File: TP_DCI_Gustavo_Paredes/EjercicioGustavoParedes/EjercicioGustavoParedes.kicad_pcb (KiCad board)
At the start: 2 copper layers, 5 parts, among them J1 Conn_01x03

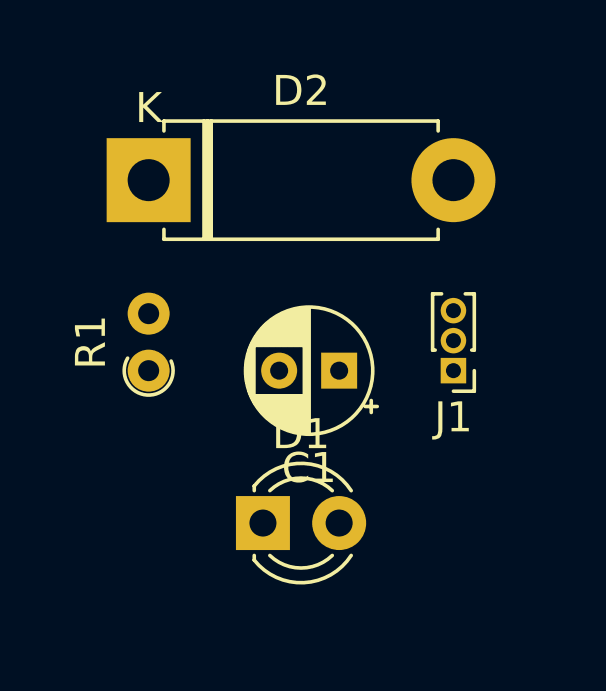
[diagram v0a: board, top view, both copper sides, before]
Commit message: Clase 5 completa
Ruteo, Puente, Recuadro.
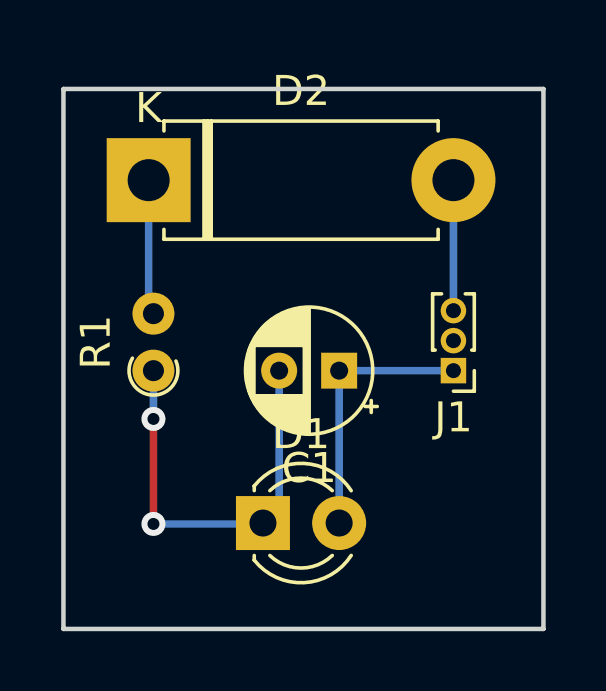
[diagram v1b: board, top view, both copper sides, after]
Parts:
- moved R1 0.16 mm to (117.0, 72.4)
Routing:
- net Net-(C1-Pad2): track 0.00 -> 14.1 mm, vias 0 -> 2
- net Net-(C1-Pad1): track 0.00 -> 8.89 mm
- net Net-(D2-Pad1): track 0.00 -> 4.52 mm
- net Net-(D2-Pad2): track 0.00 -> 4.35 mm
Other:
- board outline added: 16 x 18 mm
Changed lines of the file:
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@@
   (general
     (thickness 1.6)
-    (drawings 0)
-    (tracks 0)
+    (drawings 6)
+    (tracks 13)
     (zones 0)
     (modules 5)
@@
   (setup
     (last_trace_width 0.25)
+    (user_trace_width 0.8)
+    (user_trace_width 1)
+    (user_trace_width 1.2)
     (trace_clearance 0.2)
     (zone_clearance 0.508)
@@
     (via_min_size 0.4)
     (via_min_drill 0.3)
+    (user_via 1.6 0.8)
+    (user_via 2 0.9)
     (uvia_size 0.3)
     (uvia_drill 0.1)
@@
   )
   (module Resistor_THT:R_Axial_DIN0204_L3.6mm_D1.6mm_P1.90mm_Vertical (layer F.Cu)
-    (at 116.84 72.39 90)
+    (at 117 72.39 90)
     (descr "Resistor, Axial_DIN0204 series, Axial, Vertical, pin pitch=1.9mm, 0.167W, length*diameter=3.6*1.6mm^2, http://cdn-reichelt.de/documents/datenblatt/B400/1_4W%23YAG.pdf")
     (tags "Resistor Axial_DIN0204 series Axial Vertical pin pitch 1.9mm 0.167W length 3.6mm diameter 1.6mm")
@@
     )
   )
+  (dimension 16 (width 0.3) (layer Dwgs.User)
+    (gr_text "16,000 mm" (at 122 57.4) (layer Dwgs.User)
+      (effects (font (size 1.5 1.5) (thickness 0.3)))
+    )
+    (feature1 (pts (xy 114 63) (xy 114 58.913579)))
+    (feature2 (pts (xy 130 63) (xy 130 58.913579)))
+    (crossbar (pts (xy 130 59.5) (xy 114 59.5)))
+    (arrow1a (pts (xy 114 59.5) (xy 115.126504 58.913579)))
+    (arrow1b (pts (xy 114 59.5) (xy 115.126504 60.086421)))
+    (arrow2a (pts (xy 130 59.5) (xy 128.873496 58.913579)))
+    (arrow2b (pts (xy 130 59.5) (xy 128.873496 60.086421)))
+  )
+  (dimension 18 (width 0.3) (layer Dwgs.User)
+    (gr_text "18,000 mm" (at 135.6 72 90) (layer Dwgs.User)
+      (effects (font (size 1.5 1.5) (thickness 0.3)))
+    )
+    (feature1 (pts (xy 130 63) (xy 134.086421 63)))
+    (feature2 (pts (xy 130 81) (xy 134.086421 81)))
+    (crossbar (pts (xy 133.5 81) (xy 133.5 63)))
+    (arrow1a (pts (xy 133.5 63) (xy 134.086421 64.126504)))
+    (arrow1b (pts (xy 133.5 63) (xy 132.913579 64.126504)))
+    (arrow2a (pts (xy 133.5 81) (xy 134.086421 79.873496)))
+    (arrow2b (pts (xy 133.5 81) (xy 132.913579 79.873496)))
+  )
+  (gr_line (start 130 81) (end 114 81) (layer Edge.Cuts) (width 0.15))
+  (gr_line (start 130 63) (end 130 81) (layer Edge.Cuts) (width 0.15))
+  (gr_line (start 114 63) (end 130 63) (layer Edge.Cuts) (width 0.15))
+  (gr_line (start 114 81) (end 114 63) (layer Edge.Cuts) (width 0.15))
+  (segment (start 127 72.39) (end 123.19 72.39) (width 0.25) (layer B.Cu) (net 1))
+  (segment (start 123.19 72.39) (end 123.19 77.47) (width 0.25) (layer B.Cu) (net 1))
+  (segment (start 121.19 76.93) (end 120.65 77.47) (width 0.25) (layer B.Cu) (net 2))
+  (segment (start 121.19 72.39) (end 121.19 76.93) (width 0.25) (layer B.Cu) (net 2))
+  (via (at 117 74) (size 0.8) (drill 0.4) (layers F.Cu B.Cu) (net 2))
+  (segment (start 117 72.39) (end 117 74) (width 0.25) (layer B.Cu) (net 2))
+  (via (at 117 77.5) (size 0.8) (drill 0.4) (layers F.Cu B.Cu) (net 2))
+  (segment (start 117 74) (end 117 77.5) (width 0.25) (layer F.Cu) (net 2))
+  (segment (start 120.62 77.5) (end 120.65 77.47) (width 0.25) (layer B.Cu) (net 2))
+  (segment (start 117 77.5) (end 120.62 77.5) (width 0.25) (layer B.Cu) (net 2))
+  (segment (start 116.84 70.33) (end 117 70.49) (width 0.25) (layer B.Cu) (net 3))
+  (segment (start 116.84 66.04) (end 116.84 70.33) (width 0.25) (layer B.Cu) (net 3))
+  (segment (start 127 66.04) (end 127 70.39) (width 0.25) (layer B.Cu) (net 4))
 )
